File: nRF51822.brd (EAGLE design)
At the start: 160 x 100 mm, 14 parts

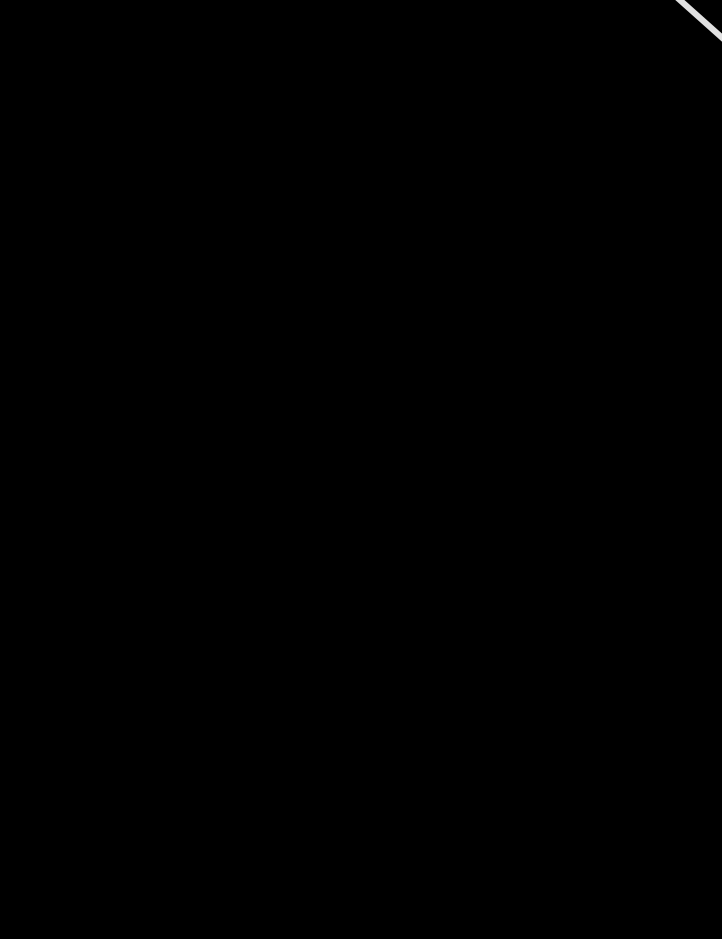
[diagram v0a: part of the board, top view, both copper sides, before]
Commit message: Agregado de mas modulos
Agregado Leds, Switchs y Alimentación
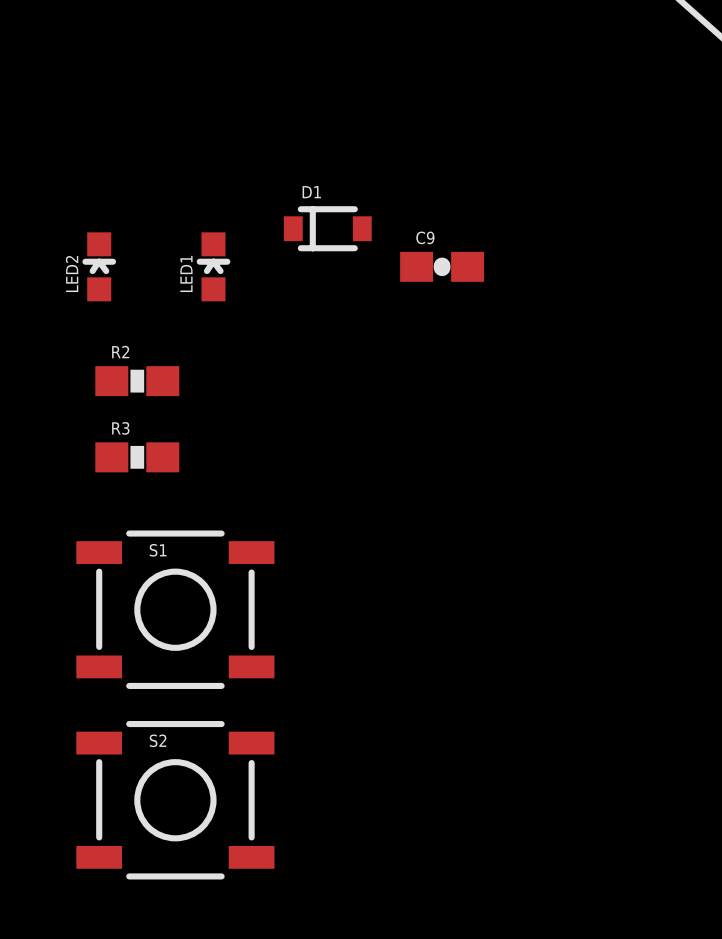
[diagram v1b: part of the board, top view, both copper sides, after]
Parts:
- added C9: 10uF, SparkFun-Capacitors:0603-CAP
- added D1: BAT165, SparkFun-DiscreteSemi:SOD-323
- added LED1, LED2: (no value), SparkFun-LED:LED-0603
- added R2, R3: 100, SparkFun-Resistors:0603-RES
- added S1, S2: (no value), SparkFun-Electromechanical:TACTILE_SWITCH_SMD
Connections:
- removed net +: BAT1.1
- removed net -: BAT1.2
- new net N$16: BAT1.1, D1.2
- new net N$18: LED2.C, R3.1
- new net N$19: LED1.C, R2.1
- new net VCC: LED1.A, LED2.A
- net GND: now also BAT1.2, C9.2, S1.1, S1.2, S2.1, S2.2
- net LED1: now also R2.2
- net LED2: now also R3.2
- net SW1: now also S1.3, S1.4
- net SW2: now also S2.3, S2.4
- net VCC_NRF: now also C9.1, D1.1
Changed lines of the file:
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@@
 <?xml version="1.0" encoding="utf-8"?>
 <!DOCTYPE eagle SYSTEM "eagle.dtd">
-<eagle version="6.4">
+<eagle version="6.2">
 <drawing>
 <settings>
@@
 </class>
 </classes>
-<designrules name="default">
+<designrules>
 <description language="de">&lt;b&gt;EAGLE Design Rules&lt;/b&gt;
 &lt;p&gt;
@@
 <element name="U$2" library="NordicSemi" package="2.5X2MM" value="CRYSTAL2.5X2" x="-35.56" y="24.13"/>
 <element name="BAT1" library="SparkFun-Electromechanical" package="BATTCON_20MM" value="" x="-29.21" y="11.43"/>
+<element name="C9" library="SparkFun-Capacitors" package="0603-CAP" value="10uF" x="-46.99" y="-2.54"/>
+<element name="D1" library="SparkFun-DiscreteSemi" package="SOD-323" value="BAT165" x="-50.8" y="-1.27"/>
+<element name="LED1" library="SparkFun-LED" package="LED-0603" value="" x="-54.61" y="-2.54"/>
+<element name="LED2" library="SparkFun-LED" package="LED-0603" value="" x="-58.42" y="-2.54"/>
+<element name="R2" library="SparkFun-Resistors" package="0603-RES" value="100" x="-57.15" y="-6.35"/>
+<element name="R3" library="SparkFun-Resistors" package="0603-RES" value="100" x="-57.15" y="-8.89"/>
+<element name="S1" library="SparkFun-Electromechanical" package="TACTILE_SWITCH_SMD" value="" x="-55.88" y="-13.97">
+<attribute name="PROD_ID" value="SWCH-08247" x="-55.88" y="-13.97" size="1.778" layer="27" display="off"/>
+</element>
+<element name="S2" library="SparkFun-Electromechanical" package="TACTILE_SWITCH_SMD" value="" x="-55.88" y="-20.32">
+<attribute name="PROD_ID" value="SWCH-08247" x="-55.88" y="-20.32" size="1.778" layer="27" display="off"/>
+</element>
 </elements>
 <signals>
-<signal name="-">
-<contactref element="BAT1" pad="2"/>
-</signal>
-<signal name="+">
-<contactref element="BAT1" pad="1"/>
-</signal>
 <signal name="N$2">
 <contactref element="L1" pad="2"/>
@@
 <contactref element="C7" pad="2"/>
 <contactref element="C8" pad="2"/>
-<wire x1="-18.2" y1="44.45" x2="-14.39" y2="44.45" width="0" layer="19" extent="1-1"/>
-<wire x1="-23.13" y1="28.73" x2="-18.2" y2="44.45" width="0" layer="19" extent="1-1"/>
-<wire x1="-23.53" y1="28.73" x2="-23.13" y2="28.73" width="0" layer="19" extent="1-1"/>
-<wire x1="-23.93" y1="28.73" x2="-23.53" y2="28.73" width="0" layer="19" extent="1-1"/>
-<wire x1="-24.33" y1="28.73" x2="-23.93" y2="28.73" width="0" layer="19" extent="1-1"/>
-<wire x1="-24.73" y1="28.73" x2="-24.33" y2="28.73" width="0" layer="19" extent="1-1"/>
-<wire x1="-22.01" y1="44.45" x2="-23.53" y2="28.73" width="0" layer="19" extent="1-1"/>
-<wire x1="-25.82" y1="44.45" x2="-24.73" y2="28.73" width="0" layer="19" extent="1-1"/>
-<wire x1="-29.63" y1="44.45" x2="-25.82" y2="44.45" width="0" layer="19" extent="1-1"/>
-<wire x1="-21.11" y1="30.35" x2="-14.39" y2="44.45" width="0" layer="19" extent="1-1"/>
-<wire x1="-21.11" y1="30.75" x2="-21.11" y2="30.35" width="0" layer="19" extent="1-1"/>
-<wire x1="-27.15" y1="30.35" x2="-29.63" y2="44.45" width="0" layer="19" extent="1-1"/>
-<wire x1="-27.15" y1="30.75" x2="-27.15" y2="30.35" width="0" layer="19" extent="1-1"/>
-<wire x1="-24.13" y1="31.75" x2="-23.93" y2="28.73" width="0" layer="19" extent="1-1"/>
-<wire x1="-42.76" y1="44.45" x2="-27.15" y2="30.35" width="0" layer="19" extent="1-1"/>
-<wire x1="-38.52" y1="24.13" x2="-27.15" y2="30.75" width="0" layer="19" extent="1-1"/>
+<contactref element="BAT1" pad="2"/>
+<contactref element="C9" pad="2"/>
+<contactref element="S1" pad="2"/>
+<contactref element="S1" pad="1"/>
+<contactref element="S2" pad="2"/>
+<contactref element="S2" pad="1"/>
+<wire x1="-53.34" y1="-18.415" x2="-58.42" y2="-18.415" width="0" layer="19" extent="1-1"/>
+<wire x1="-58.42" y1="-12.065" x2="-58.42" y2="-18.415" width="0" layer="19" extent="1-1"/>
+<wire x1="-53.34" y1="-12.065" x2="-58.42" y2="-12.065" width="0" layer="19" extent="1-1"/>
+<wire x1="-46.14" y1="-2.54" x2="-53.34" y2="-12.065" width="0" layer="19" extent="1-1"/>
+<wire x1="-29.21" y1="11.43" x2="-46.14" y2="-2.54" width="0" layer="19" extent="1-1"/>
+<wire x1="-38.52" y1="24.13" x2="-29.21" y2="11.43" width="0" layer="19" extent="1-1"/>
 <wire x1="-42.33" y1="24.13" x2="-38.52" y2="24.13" width="0" layer="19" extent="1-1"/>
 <wire x1="-46.14" y1="24.13" x2="-42.33" y2="24.13" width="0" layer="19" extent="1-1"/>
-<wire x1="-26.33" y1="34.77" x2="-38.52" y2="24.13" width="0" layer="19" extent="1-1"/>
+<wire x1="-27.15" y1="30.35" x2="-38.52" y2="24.13" width="0" layer="19" extent="1-1"/>
+<wire x1="-27.15" y1="30.75" x2="-27.15" y2="30.35" width="0" layer="19" extent="1-1"/>
+<wire x1="-24.73" y1="28.73" x2="-27.15" y2="30.35" width="0" layer="19" extent="1-1"/>
+<wire x1="-24.33" y1="28.73" x2="-24.73" y2="28.73" width="0" layer="19" extent="1-1"/>
+<wire x1="-23.93" y1="28.73" x2="-24.33" y2="28.73" width="0" layer="19" extent="1-1"/>
+<wire x1="-23.53" y1="28.73" x2="-23.93" y2="28.73" width="0" layer="19" extent="1-1"/>
+<wire x1="-23.13" y1="28.73" x2="-23.53" y2="28.73" width="0" layer="19" extent="1-1"/>
+<wire x1="-21.11" y1="30.35" x2="-23.13" y2="28.73" width="0" layer="19" extent="1-1"/>
+<wire x1="-21.11" y1="30.75" x2="-21.11" y2="30.35" width="0" layer="19" extent="1-1"/>
+<wire x1="-24.13" y1="31.75" x2="-24.33" y2="28.73" width="0" layer="19" extent="1-1"/>
+<wire x1="-26.33" y1="34.77" x2="-24.13" y2="31.75" width="0" layer="19" extent="1-1"/>
+<wire x1="-25.82" y1="44.45" x2="-26.33" y2="34.77" width="0" layer="19" extent="1-1"/>
+<wire x1="-22.01" y1="44.45" x2="-25.82" y2="44.45" width="0" layer="19" extent="1-1"/>
+<wire x1="-18.2" y1="44.45" x2="-22.01" y2="44.45" width="0" layer="19" extent="1-1"/>
+<wire x1="-14.39" y1="44.45" x2="-18.2" y2="44.45" width="0" layer="19" extent="1-1"/>
+<wire x1="-29.63" y1="44.45" x2="-25.82" y2="44.45" width="0" layer="19" extent="1-1"/>
+<wire x1="-42.76" y1="44.45" x2="-29.63" y2="44.45" width="0" layer="19" extent="1-1"/>
 </signal>
 <signal name="SWDCLK">
@@
 <signal name="LED1">
 <contactref element="U$1" pad="14"/>
+<contactref element="R2" pad="2"/>
+<wire x1="-25.93" y1="34.77" x2="-56.3" y2="-6.35" width="0" layer="19" extent="1-1"/>
 </signal>
 <signal name="LED2">
 <contactref element="U$1" pad="15"/>
+<contactref element="R3" pad="2"/>
+<wire x1="-25.53" y1="34.77" x2="-56.3" y2="-8.89" width="0" layer="19" extent="1-1"/>
 </signal>
 <signal name="N$13">
@@
 <signal name="SW1">
 <contactref element="U$1" pad="48"/>
+<contactref element="S1" pad="4"/>
+<contactref element="S1" pad="3"/>
+<wire x1="-53.34" y1="-15.875" x2="-58.42" y2="-15.875" width="0" layer="19" extent="1-1"/>
+<wire x1="-26.33" y1="28.73" x2="-53.34" y2="-15.875" width="0" layer="19" extent="1-1"/>
 </signal>
 <signal name="SW2">
 <contactref element="U$1" pad="47"/>
+<contactref element="S2" pad="3"/>
+<contactref element="S2" pad="4"/>
+<wire x1="-53.34" y1="-22.225" x2="-58.42" y2="-22.225" width="0" layer="19" extent="1-1"/>
+<wire x1="-25.93" y1="28.73" x2="-53.34" y2="-22.225" width="0" layer="19" extent="1-1"/>
 </signal>
 <signal name="AIN1">
@@
 <contactref element="C3" pad="1"/>
 <contactref element="U$1" pad="12"/>
+<contactref element="D1" pad="1"/>
+<contactref element="C9" pad="1"/>
+<wire x1="-47.84" y1="-2.54" x2="-51.95" y2="-1.27" width="0" layer="19" extent="1-1"/>
+<wire x1="-47.84" y1="24.13" x2="-51.95" y2="-1.27" width="0" layer="19" extent="1-1"/>
 <wire x1="-44.03" y1="24.13" x2="-47.84" y2="24.13" width="0" layer="19" extent="1-1"/>
-<wire x1="-27.15" y1="33.95" x2="-44.03" y2="24.13" width="0" layer="19" extent="1-1"/>
-<wire x1="-27.15" y1="29.55" x2="-27.15" y2="33.95" width="0" layer="19" extent="1-1"/>
+<wire x1="-27.15" y1="29.55" x2="-44.03" y2="24.13" width="0" layer="19" extent="1-1"/>
+<wire x1="-27.15" y1="33.95" x2="-27.15" y2="29.55" width="0" layer="19" extent="1-1"/>
 </signal>
 <signal name="N$4">
@@
 <wire x1="-33.02" y1="26.67" x2="-27.52" y2="44.45" width="0" layer="19" extent="1-1"/>
 </signal>
+<signal name="N$16">
+<contactref element="BAT1" pad="1"/>
+<contactref element="D1" pad="2"/>
+<wire x1="-41.71" y1="11.43" x2="-49.65" y2="-1.27" width="0" layer="19" extent="1-1"/>
+</signal>
+<signal name="VCC">
+<contactref element="LED1" pad="A"/>
+<contactref element="LED2" pad="A"/>
+<wire x1="-54.61" y1="-3.29" x2="-58.42" y2="-3.29" width="0" layer="19" extent="1-1"/>
+</signal>
+<signal name="N$18">
+<contactref element="LED2" pad="C"/>
+<contactref element="R3" pad="1"/>
+<wire x1="-58.42" y1="-1.79" x2="-58" y2="-8.89" width="0" layer="19" extent="1-1"/>
+</signal>
+<signal name="N$19">
+<contactref element="R2" pad="1"/>
+<contactref element="LED1" pad="C"/>
+<wire x1="-54.61" y1="-1.79" x2="-58" y2="-6.35" width="0" layer="19" extent="1-1"/>
+</signal>
 </signals>

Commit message: Update BOM
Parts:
- added JP1, JP2: M05X2SHD_SMD, SparkFun-Connectors:2X5-SHROUDED_SMD
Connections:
- new net N$17: JP2.4
- new net N$20: JP2.3
- new net N$21: JP2.5
- new net N$22: JP2.7
- new net N$23: JP2.9
- new net N$24: JP2.6
- new net N$25: JP2.8
- new net N$26: JP2.10
- net GND: now also JP1.3, JP1.5, JP1.9, JP2.2
- net SWDCLK: now also JP1.4
- net SWDIO: now also JP1.2
- net VCC: now also JP1.1, JP2.1
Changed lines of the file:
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@@
 <attribute name="PROD_ID" value="SWCH-08247" x="-55.88" y="-20.32" size="1.778" layer="27" display="off"/>
 </element>
+<element name="JP1" library="SparkFun-Connectors" package="2X5-SHROUDED_SMD" value="M05X2SHD_SMD" x="-64.77" y="-11.43"/>
+<element name="JP2" library="SparkFun-Connectors" package="2X5-SHROUDED_SMD" value="M05X2SHD_SMD" x="-74.93" y="-11.43"/>
 </elements>
 <signals>
@@
 <contactref element="S2" pad="2"/>
 <contactref element="S2" pad="1"/>
+<contactref element="JP1" pad="9"/>
+<contactref element="JP1" pad="5"/>
+<contactref element="JP1" pad="3"/>
+<contactref element="JP2" pad="2"/>
+<wire x1="-67.564" y1="-11.43" x2="-67.564" y2="-16.51" width="0" layer="19" extent="1-1"/>
+<wire x1="-67.564" y1="-8.89" x2="-67.564" y2="-11.43" width="0" layer="19" extent="1-1"/>
+<wire x1="-72.136" y1="-6.35" x2="-67.564" y2="-8.89" width="0" layer="19" extent="1-1"/>
+<wire x1="-58.42" y1="-12.065" x2="-67.564" y2="-11.43" width="0" layer="19" extent="1-1"/>
+<wire x1="-53.34" y1="-12.065" x2="-58.42" y2="-12.065" width="0" layer="19" extent="1-1"/>
+<wire x1="-58.42" y1="-18.415" x2="-58.42" y2="-12.065" width="0" layer="19" extent="1-1"/>
 <wire x1="-53.34" y1="-18.415" x2="-58.42" y2="-18.415" width="0" layer="19" extent="1-1"/>
-<wire x1="-58.42" y1="-12.065" x2="-58.42" y2="-18.415" width="0" layer="19" extent="1-1"/>
-<wire x1="-53.34" y1="-12.065" x2="-58.42" y2="-12.065" width="0" layer="19" extent="1-1"/>
 <wire x1="-46.14" y1="-2.54" x2="-53.34" y2="-12.065" width="0" layer="19" extent="1-1"/>
 <wire x1="-29.21" y1="11.43" x2="-46.14" y2="-2.54" width="0" layer="19" extent="1-1"/>
@@
 <contactref element="U$1" pad="24"/>
 <contactref element="R1" pad="2"/>
-<wire x1="-41.06" y1="44.45" x2="-21.93" y2="34.77" width="0" layer="19" extent="1-1"/>
+<contactref element="JP1" pad="4"/>
+<wire x1="-41.06" y1="44.45" x2="-61.976" y2="-8.89" width="0" layer="19" extent="1-1"/>
+<wire x1="-21.93" y1="34.77" x2="-41.06" y2="44.45" width="0" layer="19" extent="1-1"/>
 </signal>
 <signal name="LED1">
@@
 <signal name="SWDIO">
 <contactref element="U$1" pad="23"/>
+<contactref element="JP1" pad="2"/>
+<wire x1="-22.33" y1="34.77" x2="-61.976" y2="-6.35" width="0" layer="19" extent="1-1"/>
 </signal>
 <signal name="N$6">
@@
 <contactref element="LED1" pad="A"/>
 <contactref element="LED2" pad="A"/>
+<contactref element="JP1" pad="1"/>
+<contactref element="JP2" pad="1"/>
+<wire x1="-67.564" y1="-6.35" x2="-77.724" y2="-6.35" width="0" layer="19" extent="1-1"/>
+<wire x1="-58.42" y1="-3.29" x2="-67.564" y2="-6.35" width="0" layer="19" extent="1-1"/>
 <wire x1="-54.61" y1="-3.29" x2="-58.42" y2="-3.29" width="0" layer="19" extent="1-1"/>
 </signal>
@@
 <wire x1="-54.61" y1="-1.79" x2="-58" y2="-6.35" width="0" layer="19" extent="1-1"/>
 </signal>
+<signal name="N$17">
+<contactref element="JP2" pad="4"/>
+</signal>
+<signal name="N$20">
+<contactref element="JP2" pad="3"/>
+</signal>
+<signal name="N$21">
+<contactref element="JP2" pad="5"/>
+</signal>
+<signal name="N$22">
+<contactref element="JP2" pad="7"/>
+</signal>
+<signal name="N$23">
+<contactref element="JP2" pad="9"/>
+</signal>
+<signal name="N$24">
+<contactref element="JP2" pad="6"/>
+</signal>
+<signal name="N$25">
+<contactref element="JP2" pad="8"/>
+</signal>
+<signal name="N$26">
+<contactref element="JP2" pad="10"/>
+</signal>
 </signals>
